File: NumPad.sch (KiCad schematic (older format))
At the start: 50 parts, among them J1 USB_B_Micro, K1 numlk, K10 5, K11 6, K12 enter, K13 1, K14 2, K15 3, K16 0, K17 .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

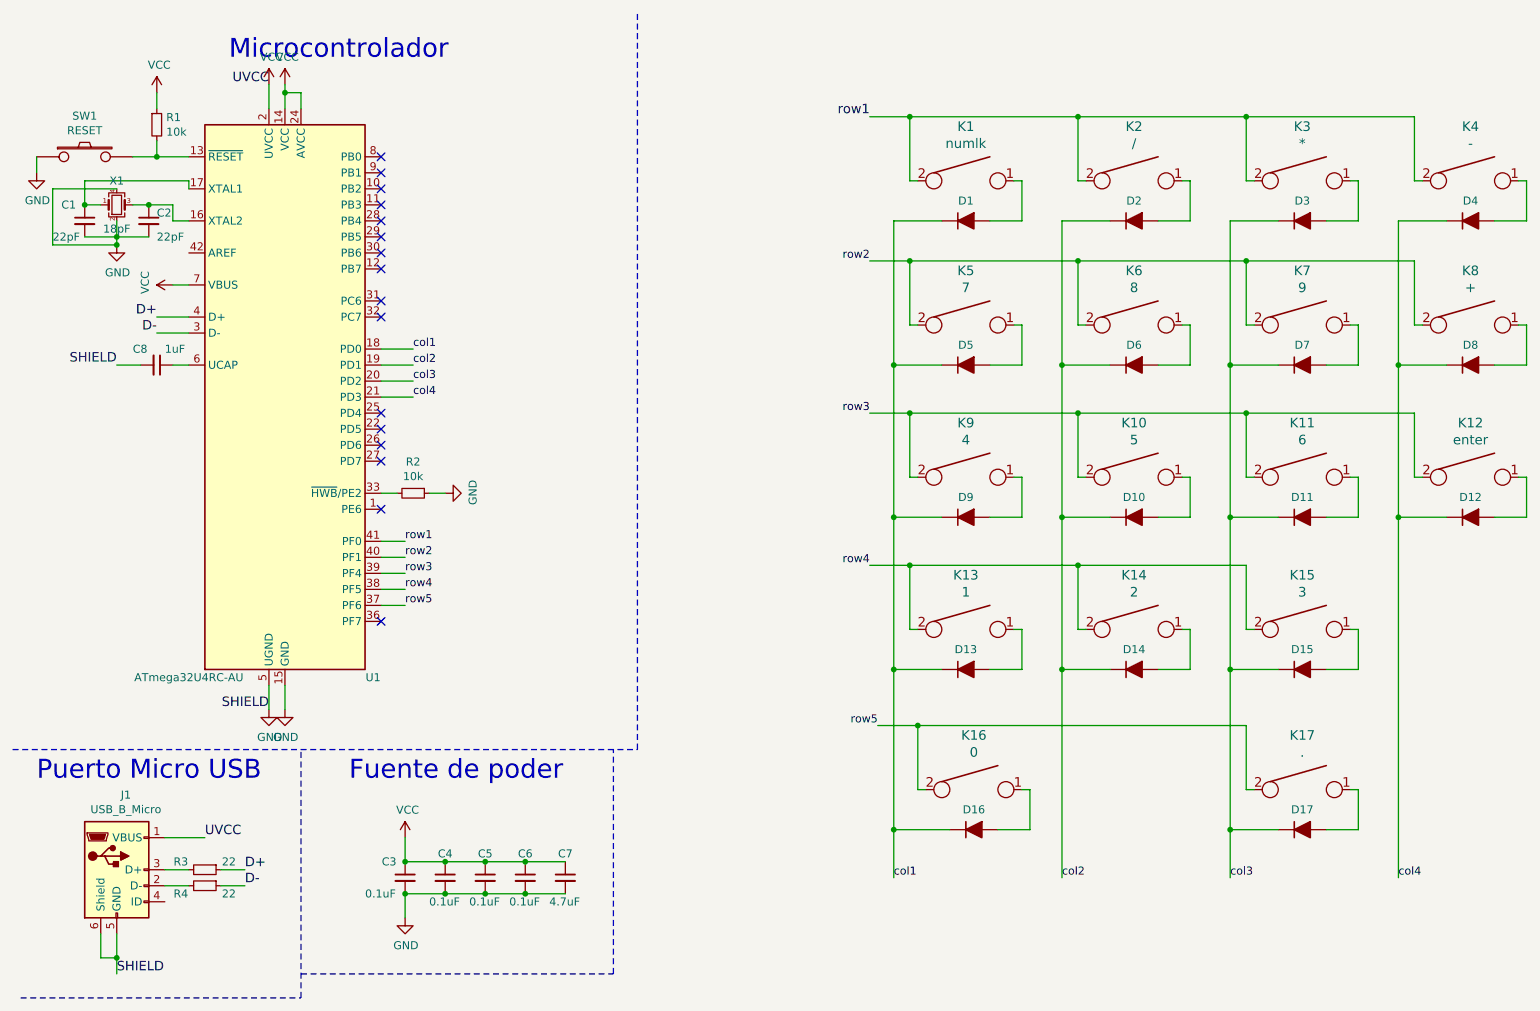
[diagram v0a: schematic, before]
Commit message: Matriz de switches del esquemático arreglada
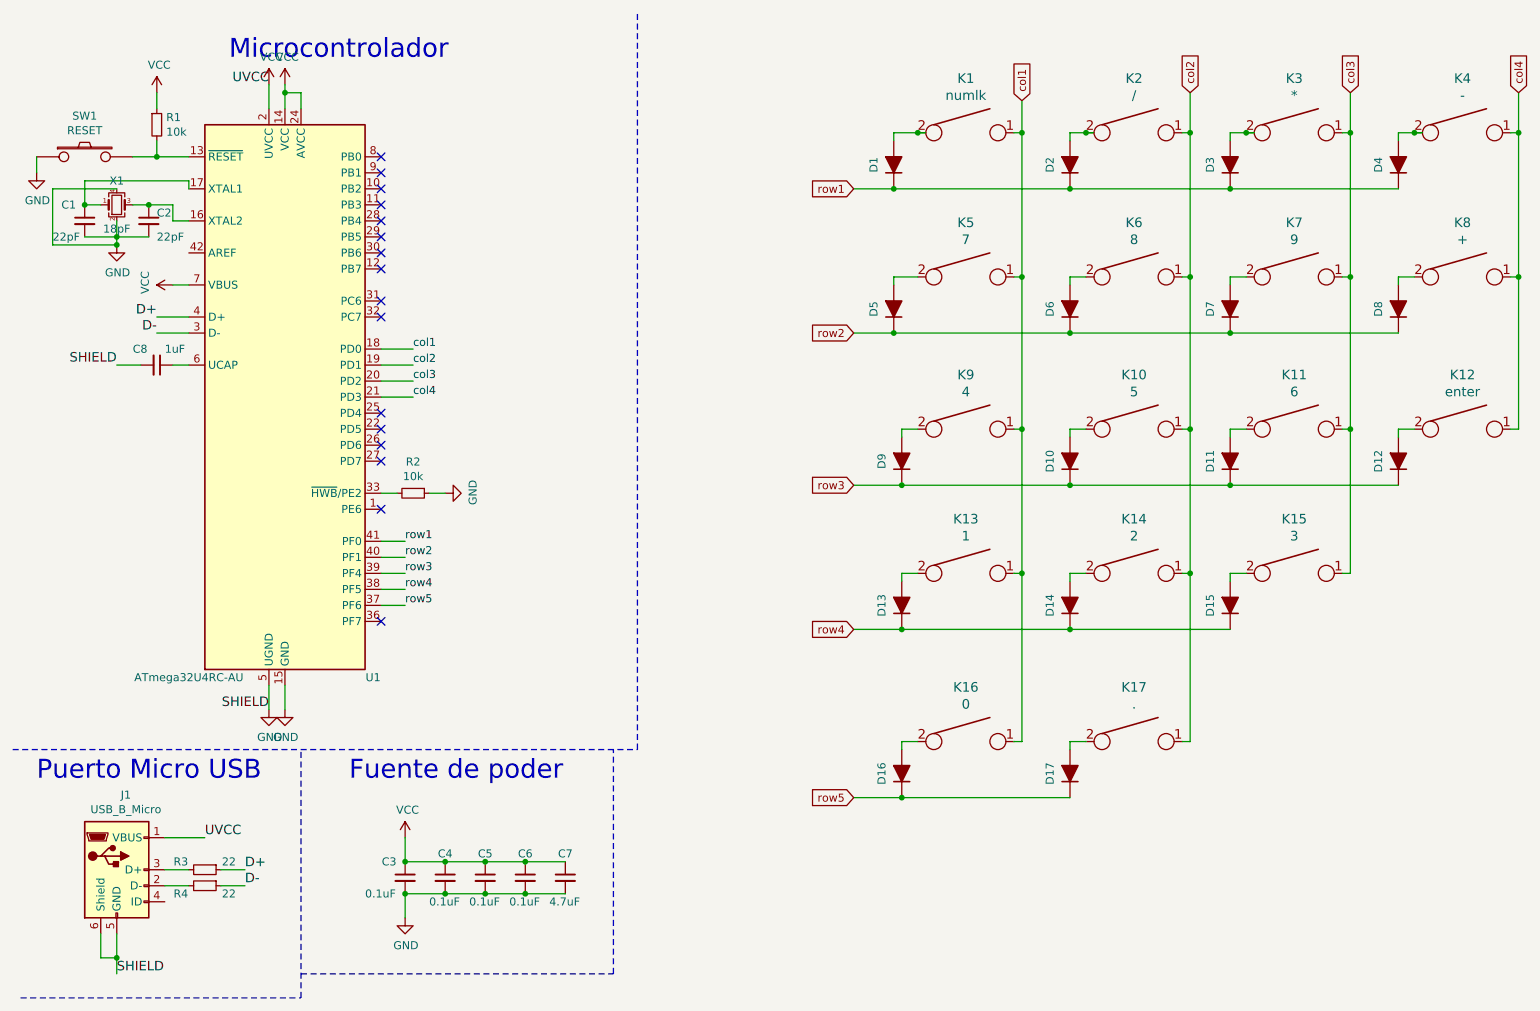
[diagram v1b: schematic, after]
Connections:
- net col1: now also K1.1, K13.1, K16.1, K5.1, K9.1; no longer D1.1 (K), D13.1 (K), D16.1 (K), D5.1 (K), D9.1 (K)
- net col2: now also K10.1, K14.1, K17.1, K2.1, K6.1; no longer D10.1 (K), D14.1 (K), D2.1 (K), D6.1 (K)
- net col3: now also K11.1, K15.1, K3.1, K7.1; no longer D11.1 (K), D15.1 (K), D17.1 (K), D3.1 (K), D7.1 (K)
- net col4: now also K12.1, K4.1, K8.1; no longer D12.1 (K), D4.1 (K), D8.1 (K)
- net row1: now also D1.1 (K), D2.1 (K), D3.1 (K), D4.1 (K); no longer K1.2, K2.2, K3.2, K4.2
- net row2: now also D5.1 (K), D6.1 (K), D7.1 (K), D8.1 (K); no longer K5.2, K6.2, K7.2, K8.2
- net row3: now also D10.1 (K), D11.1 (K), D12.1 (K), D9.1 (K); no longer K10.2, K11.2, K12.2, K9.2
- net row4: now also D13.1 (K), D14.1 (K), D15.1 (K); no longer K13.2, K14.2, K15.2
- net row5: now also D16.1 (K), D17.1 (K); no longer K16.2, K17.2
- net at D1.2 (A): now also K1.2; no longer K1.1
- net at D2.2 (A): now also K2.2; no longer K2.1
- net at D3.2 (A): now also K3.2; no longer K3.1
- net at D4.2 (A): now also K4.2; no longer K4.1
- net at D5.2 (A): now also K5.2; no longer K5.1
- net at D6.2 (A): now also K6.2; no longer K6.1
- net at D7.2 (A): now also K7.2; no longer K7.1
- net at D8.2 (A): now also K8.2; no longer K8.1
- net at D9.2 (A): now also K9.2; no longer K9.1
- net at D10.2 (A): now also K10.2; no longer K10.1
- net at D11.2 (A): now also K11.2; no longer K11.1
- net at D12.2 (A): now also K12.2; no longer K12.1
- net at D13.2 (A): now also K13.2; no longer K13.1
- net at D14.2 (A): now also K14.2; no longer K14.1
- net at D15.2 (A): now also K15.2; no longer K15.1
- net at D16.2 (A): now also K16.2; no longer K16.1
- net at D17.2 (A): now also K17.2; no longer K17.1
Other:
- moved on the sheet: D1, D10, D11, D12, D13, D14, D15, D16, D17, D2, D3, D4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

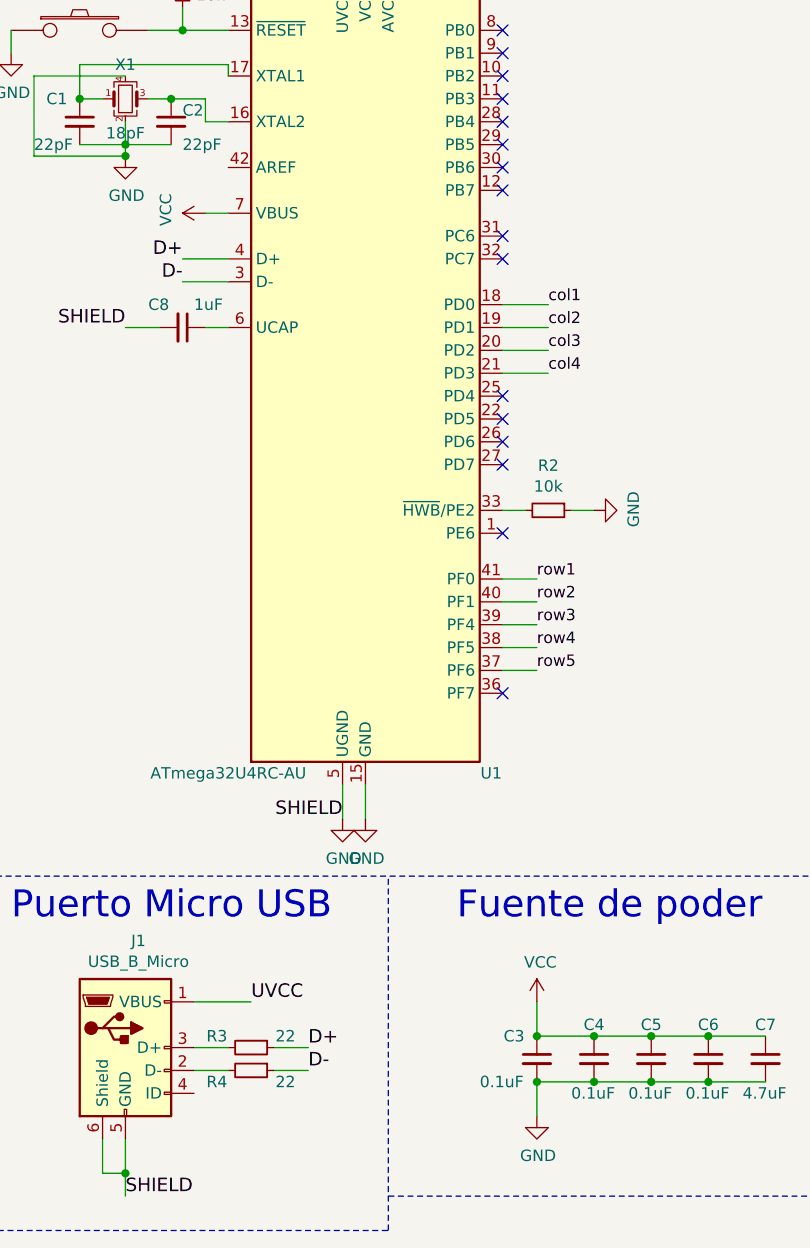
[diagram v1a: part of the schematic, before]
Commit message: Plugins añadidos y columnadas enrutadas
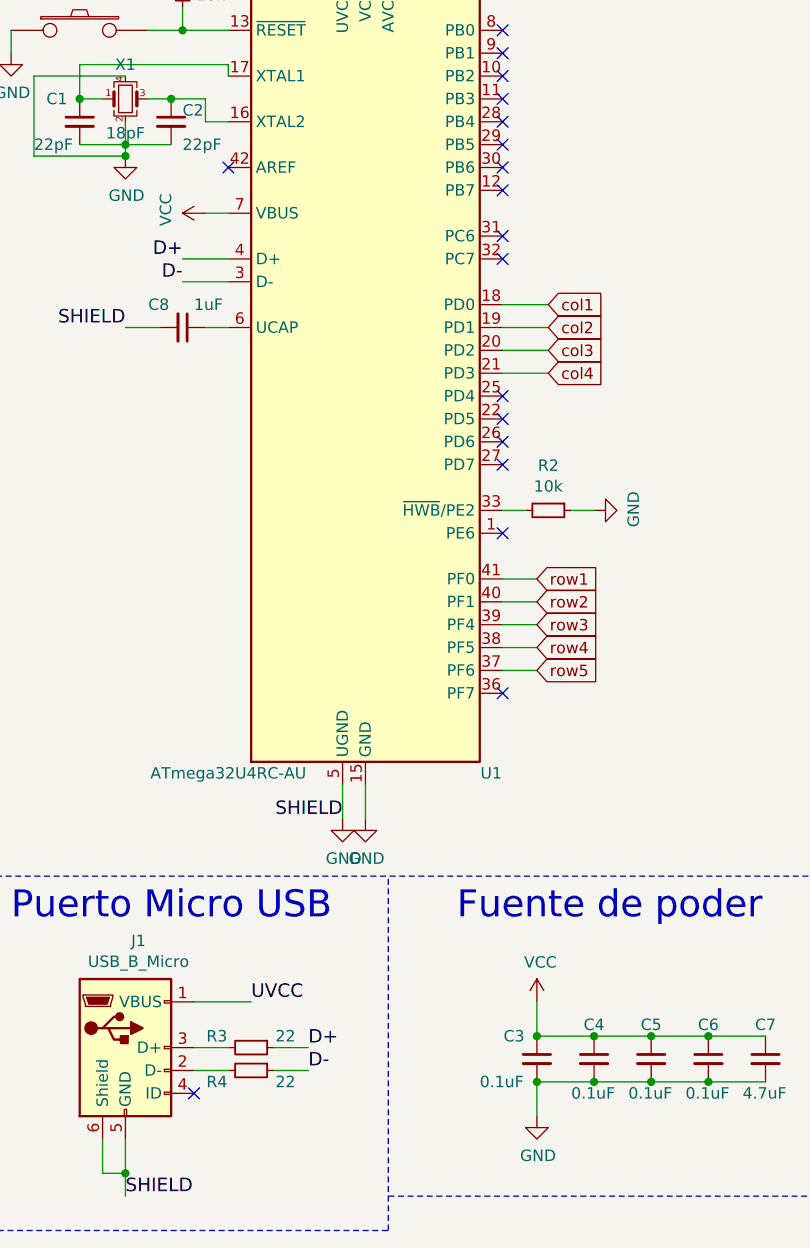
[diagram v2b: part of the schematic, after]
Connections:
- no-connect marks 16 -> 18
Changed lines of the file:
@@
 Wire Wire Line
 	3150 3450 3050 3450
-$Comp
-L Connector:USB_B_Micro J1
-U 1 1 60E84409
-P 1100 5800
-F 0 "J1" H 1157 6267 50  0000 C CNN
-F 1 "USB_B_Micro" H 1157 6176 50  0000 C CNN
-F 2 "keyboard_parts:USB_microB" H 1250 5750 50  0001 C CNN
-F 3 "~" H 1250 5750 50  0001 C CNN
-	1    1100 5800
-	1    0    0    -1
-$EndComp
 Wire Wire Line
 	1400 5600 1650 5600
@@
 Wire Wire Line
 	2750 4150 2900 4150
-Text Label 2900 3750 0    50   ~ 0
-row1
-Text Label 2900 3850 0    50   ~ 0
-row2
-Text Label 2900 3950 0    50   ~ 0
-row3
-Text Label 2900 4050 0    50   ~ 0
-row4
-Text Label 2900 4150 0    50   ~ 0
-row5
 Wire Wire Line
 	2750 2550 2950 2550
@@
 Wire Wire Line
 	2750 2850 2950 2850
-Text Label 2950 2550 0    50   ~ 0
-col1
-Text Label 2950 2650 0    50   ~ 0
-col2
-Text Label 2950 2750 0    50   ~ 0
-col3
-Text Label 2950 2850 0    50   ~ 0
-col4
 NoConn ~ 2750 4250
 NoConn ~ 2750 3550
@@
 	7050 5350 6000 5350
 Connection ~ 6000 5350
+Text GLabel 2950 2550 2    50   Input ~ 0
+col1
+Text GLabel 2950 2650 2    50   Input ~ 0
+col2
+Text GLabel 2950 2750 2    50   Input ~ 0
+col3
+Text GLabel 2950 2850 2    50   Input ~ 0
+col4
+Text GLabel 2900 3750 2    50   Input ~ 0
+row1
+Text GLabel 2900 3850 2    50   Input ~ 0
+row2
+Text GLabel 2900 3950 2    50   Input ~ 0
+row3
+Text GLabel 2900 4050 2    50   Input ~ 0
+row4
+Text GLabel 2900 4150 2    50   Input ~ 0
+row5
+$Comp
+L Connector:USB_B_Micro J1
+U 1 1 60E84409
+P 1100 5800
+F 0 "J1" H 1157 6267 50  0000 C CNN
+F 1 "USB_B_Micro" H 1157 6176 50  0000 C CNN
+F 2 "keyboard_parts:USB_microB" H 1250 5750 50  0001 C CNN
+F 3 "~" H 1250 5750 50  0001 C CNN
+	1    1100 5800
+	1    0    0    -1
+$EndComp
+NoConn ~ 1400 6000
+NoConn ~ 1550 1950
 $EndSCHEMATC

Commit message: Mas conexiones y correcion de errores.
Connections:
- net DN: now reaches J1.2 (D-), R4.2
- net DP: now reaches J1.3 (D+), R3.2
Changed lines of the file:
@@
 Wire Wire Line
 	1750 5900 1900 5900
-Text Label 1900 5800 0    59   ~ 0
-D+
-Text Label 1900 5900 0    59   ~ 0
-D-
 Wire Wire Line
 	1550 2350 1350 2350
 Wire Wire Line
 	1550 2450 1350 2450
-Text Label 1350 2350 2    59   ~ 0
-D+
-Text Label 1350 2450 2    59   ~ 0
-D-
 $Comp
 L power:GND #PWR0108
@@
 col1
 Wire Wire Line
-	5950 1250 5950 1200
-Wire Wire Line
-	5950 1200 6100 1200
-Wire Wire Line
 	5950 1550 5700 1550
 Text GLabel 5700 1550 0    50   Input ~ 0
@@
 	6750 2100 6750 1200
 Connection ~ 6750 1200
-Connection ~ 6100 1200
-Wire Wire Line
-	6100 1200 6150 1200
 Wire Wire Line
 	6700 1200 6750 1200
@@
 row2
 Wire Wire Line
-	7050 1250 7050 1200
-Wire Wire Line
-	7050 1200 7150 1200
-Wire Wire Line
 	7050 1550 5950 1550
 Connection ~ 5950 1550
@@
 Connection ~ 7050 1550
 Wire Wire Line
-	8050 1250 8050 1200
-Wire Wire Line
-	8050 1200 8150 1200
-Wire Wire Line
 	9100 1550 8050 1550
 Connection ~ 8050 1550
-Wire Wire Line
-	9100 1250 9100 1200
-Wire Wire Line
-	9100 1200 9200 1200
 Wire Wire Line
 	8800 1200 8800 950
@@
 Wire Wire Line
 	7050 2150 7050 2100
-Connection ~ 7150 1200
-Wire Wire Line
-	7150 1200 7200 1200
-Connection ~ 8150 1200
-Wire Wire Line
-	8150 1200 8200 1200
-Connection ~ 9200 1200
-Wire Wire Line
-	9200 1200 9250 1200
 Wire Wire Line
 	8800 1200 8750 1200
@@
 NoConn ~ 1400 6000
 NoConn ~ 1550 1950
+Text Label 1350 2450 2    59   ~ 0
+D-
+Text Label 1350 2350 2    59   ~ 0
+D+
+Text Label 1900 5900 0    59   ~ 0
+D-
+Text Label 1900 5800 0    59   ~ 0
+D+
+Text GLabel 1450 5800 1    50   Input ~ 0
+DP
+Text GLabel 1450 5900 3    50   Input ~ 0
+DN
+Wire Wire Line
+	5950 1250 5950 1200
+Wire Wire Line
+	5950 1200 6100 1200
+Wire Wire Line
+	7050 1250 7050 1200
+Wire Wire Line
+	7050 1200 7150 1200
+Wire Wire Line
+	8050 1250 8050 1200
+Wire Wire Line
+	8050 1200 8150 1200
+Wire Wire Line
+	9100 1250 9100 1200
+Wire Wire Line
+	9100 1200 9200 1200
 $EndSCHEMATC
